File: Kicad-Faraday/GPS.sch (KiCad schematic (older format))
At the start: 19 parts, among them U7 M10478-A2

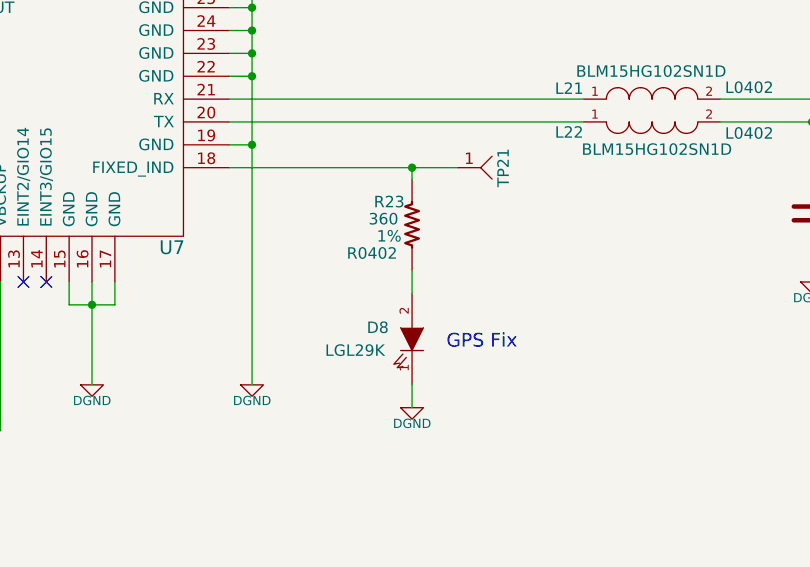
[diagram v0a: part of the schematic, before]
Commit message: Removed basic parts I don't really need to test or am so confident that testing will be fine I'm OK making the changes well in advance
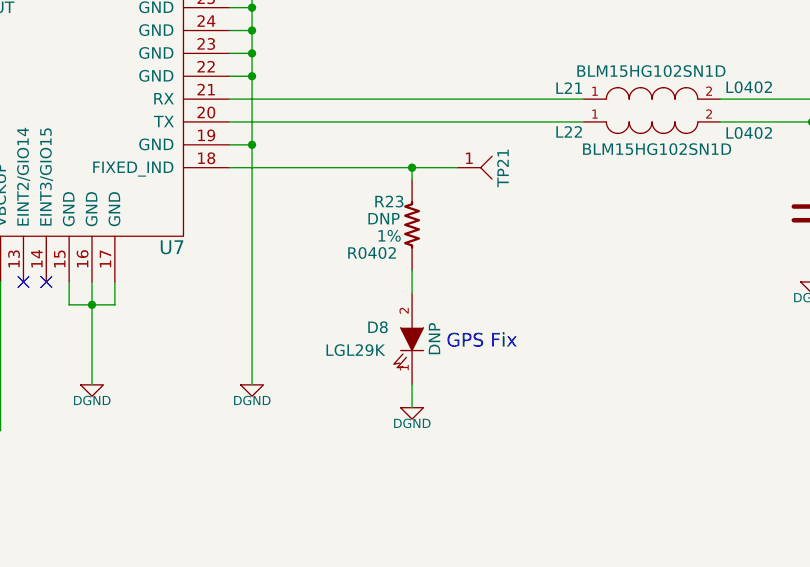
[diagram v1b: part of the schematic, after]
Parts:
- D8: value LED-IPC -> DNP
- R23: value 360 -> DNP
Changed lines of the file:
@@
 Sheet 9 11
 Title "Faraday Wireless Node"
-Date "24 oct 2016"
+Date "2 nov 2016"
 Rev "C"
 Comp "FaradayRF"
@@
 PPS
 $Comp
-L +3.3V #PWR091
+L +3.3V #PWR090
 U 1 1 54FE8E93
 P 6000 4750
-F 0 "#PWR091" H 6000 4710 30  0001 C CNN
+F 0 "#PWR090" H 6000 4710 30  0001 C CNN
 F 1 "+3.3V" H 6000 4860 30  0000 C CNN
 F 2 "" H 6000 4750 60  0000 C CNN
@@
 $EndComp
 $Comp
-L DGND #PWR092
+L DGND #PWR091
 U 1 1 55A57931
 P 7200 6000
-F 0 "#PWR092" H 7200 6000 40  0001 C CNN
+F 0 "#PWR091" H 7200 6000 40  0001 C CNN
 F 1 "DGND" H 7200 5930 40  0000 C CNN
 F 2 "~" H 7200 6000 60  0000 C CNN
@@
 $EndComp
 $Comp
-L DGND #PWR093
+L DGND #PWR092
 U 1 1 55C1D944
 P 8900 6000
-F 0 "#PWR093" H 8900 6000 40  0001 C CNN
+F 0 "#PWR092" H 8900 6000 40  0001 C CNN
 F 1 "DGND" H 8900 5930 40  0000 C CNN
 F 2 "~" H 8900 6000 60  0000 C CNN
@@
 $EndComp
 $Comp
-L DGND #PWR094
+L DGND #PWR093
 U 1 1 55C1DDA1
 P 8200 6000
-F 0 "#PWR094" H 8200 6000 40  0001 C CNN
+F 0 "#PWR093" H 8200 6000 40  0001 C CNN
 F 1 "DGND" H 8200 5930 40  0000 C CNN
 F 2 "~" H 8200 6000 60  0000 C CNN
@@
 $EndComp
 $Comp
-L DGND #PWR095
+L DGND #PWR094
 U 1 1 55C1E57A
 P 6100 5800
-F 0 "#PWR095" H 6100 5800 40  0001 C CNN
+F 0 "#PWR094" H 6100 5800 40  0001 C CNN
 F 1 "DGND" H 6100 5730 40  0000 C CNN
 F 2 "~" H 6100 5800 60  0000 C CNN
@@
 $EndComp
 $Comp
-L DGND #PWR096
+L DGND #PWR095
 U 1 1 55C1FC6F
 P 11350 5550
-F 0 "#PWR096" H 11350 5550 40  0001 C CNN
+F 0 "#PWR095" H 11350 5550 40  0001 C CNN
 F 1 "DGND" H 11350 5480 40  0000 C CNN
 F 2 "~" H 11350 5550 60  0000 C CNN
@@
 $EndComp
 $Comp
-L DGND #PWR097
+L DGND #PWR096
 U 1 1 55C1FC7E
 P 11900 5550
-F 0 "#PWR097" H 11900 5550 40  0001 C CNN
+F 0 "#PWR096" H 11900 5550 40  0001 C CNN
 F 1 "DGND" H 11900 5480 40  0000 C CNN
 F 2 "~" H 11900 5550 60  0000 C CNN
@@
 $EndComp
 $Comp
-L DGND #PWR098
+L DGND #PWR097
 U 1 1 55C2116E
 P 6450 2900
-F 0 "#PWR098" H 6450 2900 40  0001 C CNN
+F 0 "#PWR097" H 6450 2900 40  0001 C CNN
 F 1 "DGND" H 6450 2830 40  0000 C CNN
 F 2 "~" H 6450 2900 60  0000 C CNN
@@
 $EndComp
 $Comp
-L DGND #PWR099
+L DGND #PWR098
 U 1 1 55C21174
 P 6850 2900
-F 0 "#PWR099" H 6850 2900 40  0001 C CNN
+F 0 "#PWR098" H 6850 2900 40  0001 C CNN
 F 1 "DGND" H 6850 2830 40  0000 C CNN
 F 2 "~" H 6850 2900 60  0000 C CNN
@@
 $EndComp
 $Comp
-L DGND #PWR0100
+L DGND #PWR099
 U 1 1 55C26F32
 P 12450 5550
-F 0 "#PWR0100" H 12450 5550 40  0001 C CNN
+F 0 "#PWR099" H 12450 5550 40  0001 C CNN
 F 1 "DGND" H 12450 5480 40  0000 C CNN
 F 2 "~" H 12450 5550 60  0000 C CNN
@@
 P 9600 5300
 F 0 "R23" H 9500 5400 50  0000 C CNN
-F 1 "360" H 9475 5325 50  0000 C CNN
+F 1 "DNP" H 9475 5325 50  0000 C CNN
 F 2 "R0402" H 9425 5175 50  0000 C CNN
 F 3 "" H 9600 5300 60  0000 C CNN
@@
 GPS Fix
 $Comp
-L DGND #PWR0101
+L DGND #PWR0100
 U 1 1 55C46E4B
 P 9600 6100
-F 0 "#PWR0101" H 9600 6100 40  0001 C CNN
+F 0 "#PWR0100" H 9600 6100 40  0001 C CNN
 F 1 "DGND" H 9600 6030 40  0000 C CNN
 F 2 "~" H 9600 6100 60  0000 C CNN
@@
 $EndComp
 $Comp
-L DGND #PWR0102
+L DGND #PWR0101
 U 1 1 578BCA89
 P 4500 5800
-F 0 "#PWR0102" H 4500 5800 40  0001 C CNN
+F 0 "#PWR0101" H 4500 5800 40  0001 C CNN
 F 1 "DGND" H 4500 5730 40  0000 C CNN
 F 2 "~" H 4500 5800 60  0000 C CNN
@@
 $EndComp
 $Comp
-L DGND #PWR0103
+L DGND #PWR0102
 U 1 1 578BCA98
 P 4975 5800
-F 0 "#PWR0103" H 4975 5800 40  0001 C CNN
+F 0 "#PWR0102" H 4975 5800 40  0001 C CNN
 F 1 "DGND" H 4975 5730 40  0000 C CNN
 F 2 "~" H 4975 5800 60  0000 C CNN
@@
 P 9600 5800
 F 0 "D8" V 9550 5650 50  0000 C CNN
-F 1 "LED-IPC" H 9600 5700 50  0001 C CNN
+F 1 "DNP" H 9600 5900 50  0000 C CNN
 F 2 "LGL29K" V 9650 5550 50  0000 C CNN
 F 3 "~" H 9600 5800 60  0000 C CNN
